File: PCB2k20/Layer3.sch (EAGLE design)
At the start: 57 parts, among them J1 14AWG, J2 CONN_03, J3 14AWG, J4 14AWG, J6 14AWG, X1 BM10B-SRSS-TB

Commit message: add gerbers, please everything turn out well!
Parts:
- added D1: BLUE, SparkFun-LED:LED-BLUE0603
- added R11: 1k, JH:RESISTOR0603
- 2L1: value SWPA8040/10uH -> 10uH
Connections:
- new net N$13: R11.2, RPI_UART.4
- new net N$14: D1.A, R11.1
- net GND: now also D1.C
- net IMU_RST: now also 1U1.PC13-TAMPER-RTC
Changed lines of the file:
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@@
 <part name="2C3" library="JH" library_urn="urn:adsk.eagle:library:6027132" deviceset="CAPACITOR" device="0603" package3d_urn="urn:adsk.eagle:package:15441226/3" value="10.0nF"/>
 <part name="2D1" library="SparkFun-DiscreteSemi" library_urn="urn:adsk.eagle:library:514" deviceset="DIODE-SCHOTTKY" device="-B340A" package3d_urn="urn:adsk.eagle:package:38443/1" value="3A/40V/500mV"/>
-<part name="2L1" library="JH" library_urn="urn:adsk.eagle:library:6027132" deviceset="INDUCTOR" device="SWPA8040" package3d_urn="urn:adsk.eagle:package:15402033/4" value="SWPA8040/10uH"/>
+<part name="2L1" library="JH" library_urn="urn:adsk.eagle:library:6027132" deviceset="INDUCTOR" device="SWPA8040" package3d_urn="urn:adsk.eagle:package:15402033/4" value="10uH"/>
 <part name="2R1" library="JH" library_urn="urn:adsk.eagle:library:6027132" deviceset="RESISTOR" device="0603" package3d_urn="urn:adsk.eagle:package:15441228/3" value="10k"/>
 <part name="2C4" library="rcl" library_urn="urn:adsk.eagle:library:334" deviceset="CPOL-US" device="D/7343-31R" package3d_urn="urn:adsk.eagle:package:23417/2" value="220uF"/>
@@
 <part name="J4" library="JH" library_urn="urn:adsk.eagle:library:6027132" deviceset="14AWG" device="" package3d_urn="urn:adsk.eagle:package:16673531/1"/>
 <part name="J6" library="JH" library_urn="urn:adsk.eagle:library:6027132" deviceset="14AWG" device="" package3d_urn="urn:adsk.eagle:package:16673531/1"/>
+<part name="R11" library="JH" library_urn="urn:adsk.eagle:library:6027132" deviceset="RESISTOR" device="0603" package3d_urn="urn:adsk.eagle:package:15441228/3" value="1k"/>
+<part name="SUPPLY3" library="SparkFun-PowerSymbols" library_urn="urn:adsk.eagle:library:530" deviceset="GND" device="" value="GND"/>
+<part name="D1" library="SparkFun-LED" library_urn="urn:adsk.eagle:library:529" deviceset="LED-BLUE" device="0603" package3d_urn="urn:adsk.eagle:package:39354/1" value="BLUE"/>
 </parts>
 <sheets>
@@
 <attribute name="VALUE" x="241.3" y="91.186" size="1.778" layer="96" font="vector" rot="R180"/>
 <attribute name="NAME" x="241.3" y="83.312" size="1.778" layer="95" font="vector" rot="R180"/>
+</instance>
+<instance part="R11" gate="G$1" x="200.66" y="78.74" smashed="yes" rot="MR0">
+<attribute name="NAME" x="202.7174" y="73.406" size="1.778" layer="95" rot="R90"/>
+<attribute name="VALUE" x="201.168" y="83.058" size="1.778" layer="96" rot="R270"/>
+</instance>
+<instance part="SUPPLY3" gate="1" x="220.98" y="78.74" smashed="yes" rot="R90">
+<attribute name="VALUE" x="224.155" y="76.073" size="1.778" layer="96" rot="R90"/>
+</instance>
+<instance part="D1" gate="G$1" x="210.82" y="78.74" smashed="yes" rot="R90">
+<attribute name="NAME" x="215.392" y="75.311" size="1.778" layer="95" font="vector" rot="R180"/>
+<attribute name="VALUE" x="215.392" y="80.645" size="1.778" layer="96" font="vector" rot="R180" align="top-left"/>
 </instance>
 </instances>
@@
 <junction x="10.16" y="50.8"/>
 </segment>
+<segment>
+<wire x1="215.9" y1="78.74" x2="218.44" y2="78.74" width="0.1524" layer="91"/>
+<pinref part="SUPPLY3" gate="1" pin="GND"/>
+<pinref part="D1" gate="G$1" pin="C"/>
+</segment>
 </net>
 <net name="BT_RX" class="0">
@@
 <pinref part="R9" gate="G$1" pin="1"/>
 <wire x1="40.64" y1="66.04" x2="40.64" y2="53.34" width="0.1524" layer="91"/>
+</segment>
+</net>
+<net name="N$13" class="0">
+<segment>
+<pinref part="RPI_UART" gate="G$1" pin="4"/>
+<wire x1="187.96" y1="78.74" x2="195.58" y2="78.74" width="0.1524" layer="91"/>
+<pinref part="R11" gate="G$1" pin="2"/>
+</segment>
+</net>
+<net name="N$14" class="0">
+<segment>
+<wire x1="205.74" y1="78.74" x2="208.28" y2="78.74" width="0.1524" layer="91"/>
+<pinref part="R11" gate="G$1" pin="1"/>
+<pinref part="D1" gate="G$1" pin="A"/>
 </segment>
 </net>
@@
 </segment>
 </net>
+<net name="IMU_RST" class="0">
+<segment>
+<pinref part="1U1" gate="G$1" pin="PC13-TAMPER-RTC"/>
+<wire x1="114.3" y1="101.6" x2="104.14" y2="101.6" width="0.1524" layer="91"/>
+<label x="104.14" y="101.6" size="1.778" layer="95"/>
+</segment>
+</net>

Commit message: update values
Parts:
- R1: value 300k -> 30k
- R10, R3, R4, R5, R8, R9: value (none) -> 10k
- R2: value 100k -> 10k
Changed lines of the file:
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@@
 <drawing>
 <settings>
-<setting alwaysvectorfont="yes"/>
+<setting alwaysvectorfont="no"/>
 <setting verticaltext="up"/>
 </settings>
@@
 <part name="GND2" library="SparkFun-PowerSymbols" library_urn="urn:adsk.eagle:library:530" deviceset="GND" device=""/>
 <part name="SUPPLY1" library="SparkFun-PowerSymbols" library_urn="urn:adsk.eagle:library:530" deviceset="5V" device=""/>
-<part name="R1" library="JH" library_urn="urn:adsk.eagle:library:6027132" deviceset="RESISTOR" device="0603" package3d_urn="urn:adsk.eagle:package:15441228/3" value="300k"/>
-<part name="R2" library="JH" library_urn="urn:adsk.eagle:library:6027132" deviceset="RESISTOR" device="0603" package3d_urn="urn:adsk.eagle:package:15441228/3" value="100k"/>
+<part name="R1" library="JH" library_urn="urn:adsk.eagle:library:6027132" deviceset="RESISTOR" device="0603" package3d_urn="urn:adsk.eagle:package:15441228/3" value="30k"/>
+<part name="R2" library="JH" library_urn="urn:adsk.eagle:library:6027132" deviceset="RESISTOR" device="0603" package3d_urn="urn:adsk.eagle:package:15441228/3" value="10k"/>
 <part name="R6" library="JH" library_urn="urn:adsk.eagle:library:6027132" deviceset="RESISTOR" device="0603" package3d_urn="urn:adsk.eagle:package:15441228/3"/>
 <part name="R7" library="JH" library_urn="urn:adsk.eagle:library:6027132" deviceset="RESISTOR" device="0603" package3d_urn="urn:adsk.eagle:package:15441228/3"/>
@@
 <part name="J2" library="JH" library_urn="urn:adsk.eagle:library:6027132" deviceset="CONN_03" device="" package3d_urn="urn:adsk.eagle:package:15924798/2"/>
 <part name="GND3" library="SparkFun-PowerSymbols" deviceset="GND" device=""/>
-<part name="R3" library="JH" library_urn="urn:adsk.eagle:library:6027132" deviceset="RESISTOR" device="0603" package3d_urn="urn:adsk.eagle:package:15441228/3"/>
-<part name="R4" library="JH" library_urn="urn:adsk.eagle:library:6027132" deviceset="RESISTOR" device="0603" package3d_urn="urn:adsk.eagle:package:15441228/3"/>
-<part name="R5" library="JH" library_urn="urn:adsk.eagle:library:6027132" deviceset="RESISTOR" device="0603" package3d_urn="urn:adsk.eagle:package:15441228/3"/>
-<part name="R8" library="JH" library_urn="urn:adsk.eagle:library:6027132" deviceset="RESISTOR" device="0603" package3d_urn="urn:adsk.eagle:package:15441228/3"/>
-<part name="R9" library="JH" library_urn="urn:adsk.eagle:library:6027132" deviceset="RESISTOR" device="0603" package3d_urn="urn:adsk.eagle:package:15441228/3"/>
-<part name="R10" library="JH" library_urn="urn:adsk.eagle:library:6027132" deviceset="RESISTOR" device="0603" package3d_urn="urn:adsk.eagle:package:15441228/3"/>
+<part name="R3" library="JH" library_urn="urn:adsk.eagle:library:6027132" deviceset="RESISTOR" device="0603" package3d_urn="urn:adsk.eagle:package:15441228/3" value="10k"/>
+<part name="R4" library="JH" library_urn="urn:adsk.eagle:library:6027132" deviceset="RESISTOR" device="0603" package3d_urn="urn:adsk.eagle:package:15441228/3" value="10k"/>
+<part name="R5" library="JH" library_urn="urn:adsk.eagle:library:6027132" deviceset="RESISTOR" device="0603" package3d_urn="urn:adsk.eagle:package:15441228/3" value="10k"/>
+<part name="R8" library="JH" library_urn="urn:adsk.eagle:library:6027132" deviceset="RESISTOR" device="0603" package3d_urn="urn:adsk.eagle:package:15441228/3" value="10k"/>
+<part name="R9" library="JH" library_urn="urn:adsk.eagle:library:6027132" deviceset="RESISTOR" device="0603" package3d_urn="urn:adsk.eagle:package:15441228/3" value="10k"/>
+<part name="R10" library="JH" library_urn="urn:adsk.eagle:library:6027132" deviceset="RESISTOR" device="0603" package3d_urn="urn:adsk.eagle:package:15441228/3" value="10k"/>
 <part name="SUPPLY2" library="SparkFun-PowerSymbols" library_urn="urn:adsk.eagle:library:530" deviceset="3.3V" device=""/>
 <part name="J1" library="JH" library_urn="urn:adsk.eagle:library:6027132" deviceset="14AWG" device="" package3d_urn="urn:adsk.eagle:package:16673531/1"/>

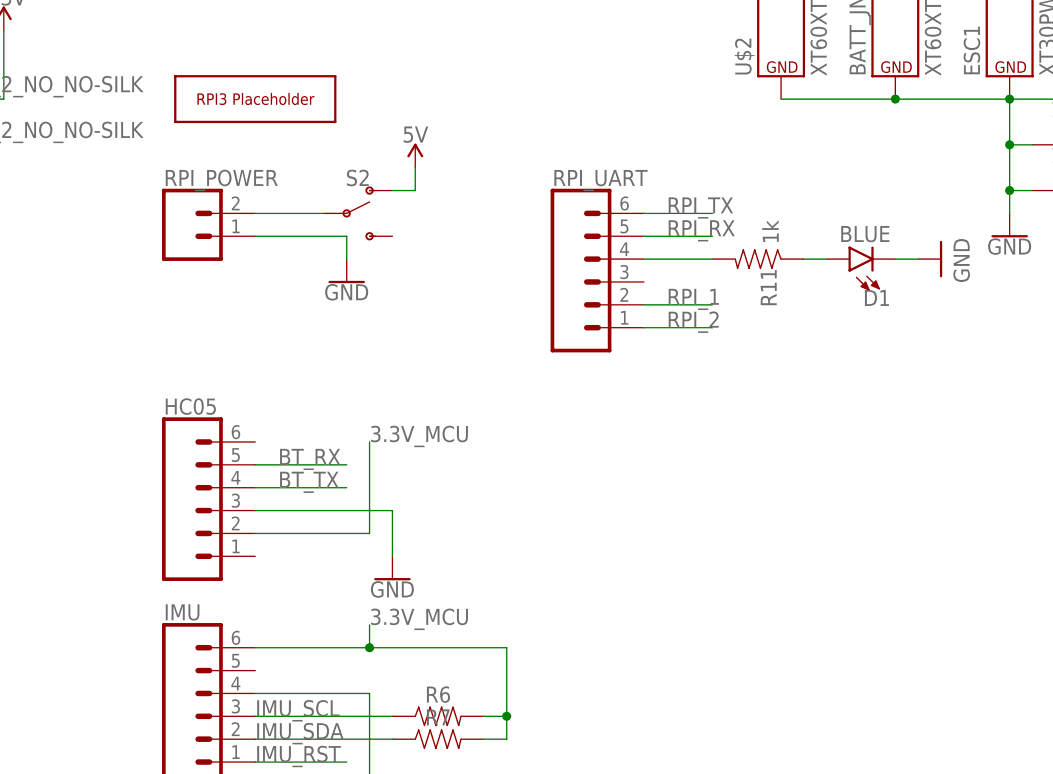
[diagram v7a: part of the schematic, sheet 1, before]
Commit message: BROKEN VERSION for 3d models
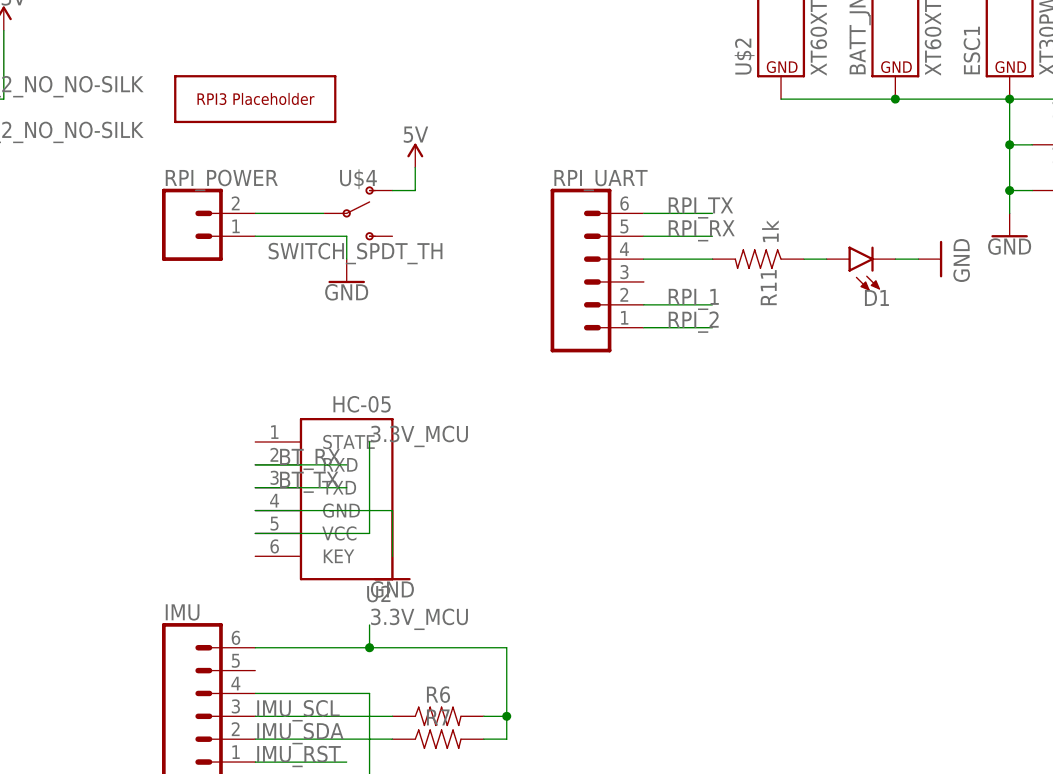
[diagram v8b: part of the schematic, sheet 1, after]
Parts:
- removed HC05: (no value), SparkFun-Connectors:CONN_06RA_LOCK
- removed S2, S3: (no value), SparkFun-Switches:SWITCH-SPDT-PTH-11.6X4.0MM-LOCK
- added U$3, U$4: SWITCH_SPDT_TH, JH:SWITCH_SPDT_TH
- added U2: HC-05_BENT, JH:HC-05_BENT
- 1D1, D1: device SparkFun-LED:LED-BLUE0603 -> JH:LED0603
- 1OSC: device SparkFun-Clocks:CRYSTALSMD-5X3.2-2PAD -> JH:CRYSTAL_5032
- 2D1: device SparkFun-DiscreteSemi:DIODE-SCHOTTKY-B340A -> JH:DIODE-SCHOTTKY
- J5: device SparkFun-Connectors:CONN_05LOCK -> Connectors:CONN_05LOCK
- RPI_POWER: device SparkFun-Connectors:CONN_02LOCK -> Connectors:CONN_02LOCK
- RPI_UART: device SparkFun-Connectors:CONN_06LOCK -> Connectors:CONN_06LOCK
- S1: device SparkFun-Switches:DIP-06 -> JH:DIP-06
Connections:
- net 3.3V: now also U$3.O; no longer S3.O
- net 3.3V_MCU: now also U$3.P, U2.VCC; no longer HC05.2, S3.P
- net 3.3V_PROG: now also U$3.S; no longer S3.S
- net 5V: now also U$4.O; no longer S2.O
- net BT_RX: now also U2.RXD; no longer HC05.5
- net BT_TX: now also U2.TXD; no longer HC05.4
- net GND: now also U2.GND; no longer HC05.3
- net N$9: now also U$4.P; no longer S2.P
